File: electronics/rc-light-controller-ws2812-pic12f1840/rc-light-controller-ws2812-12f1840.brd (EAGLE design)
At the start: 33.7 x 10.2 mm, 13 parts, among them U1 12F1840

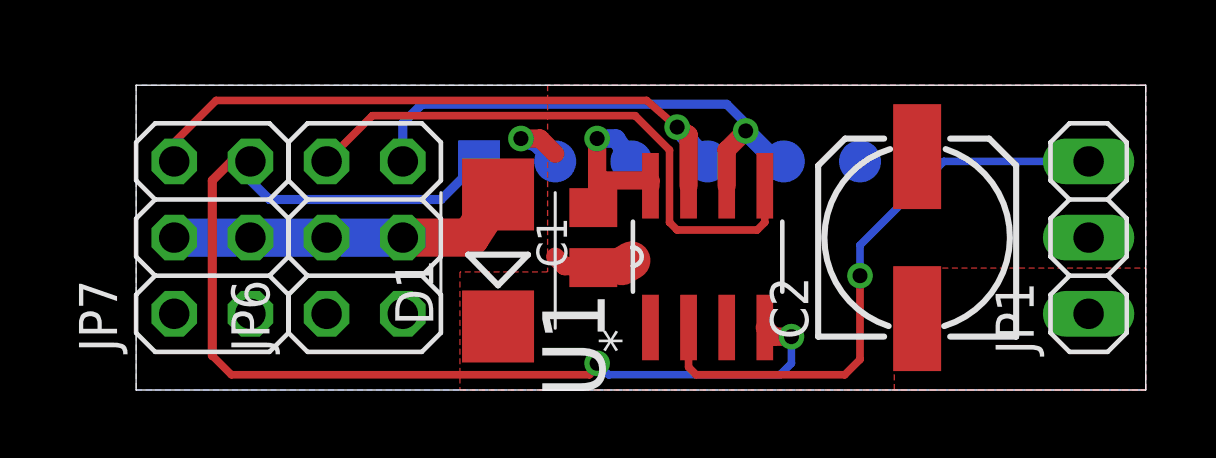
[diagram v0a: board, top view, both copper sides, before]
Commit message: Finish breakout board, tweak light controller board
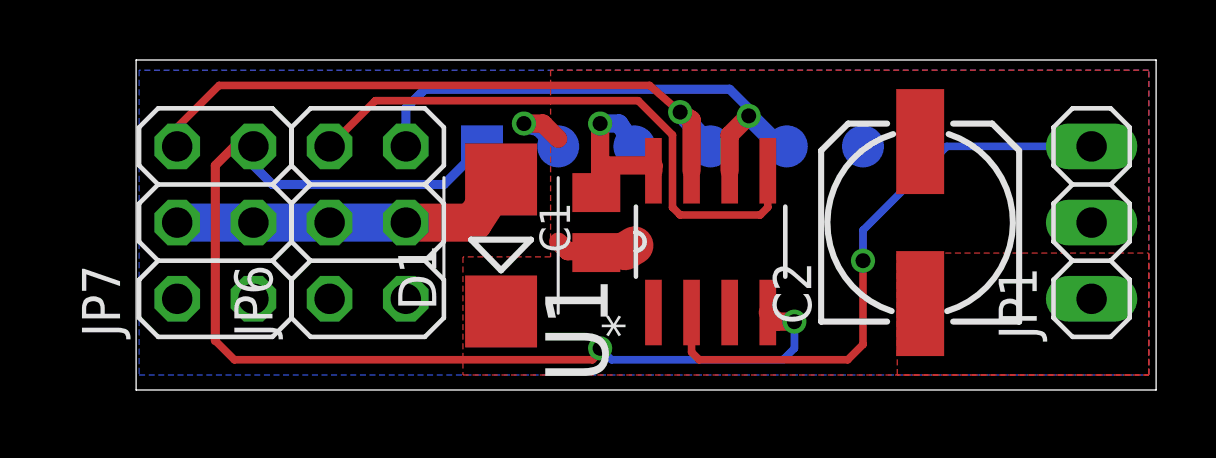
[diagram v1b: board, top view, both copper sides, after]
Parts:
- moved C2 0.51 mm to (26.1, 5.58)
- moved JP1 0.51 mm to (31.9, 5.58)
- moved JP7 0.51 mm to (2.64, 5.58)
- moved C1 0.51 mm to (15.3, 5.58)
- moved D1 0.51 mm to (12.2, 4.82)
- moved JP6 0.51 mm to (7.72, 5.58)
- moved U1 0.51 mm to (19.1, 4.95)
- moved CLK 0.51 mm to (21.7, 8.12)
- moved NC 0.51 mm to (24.2, 8.12)
- moved VDD 0.51 mm to (14.1, 8.12)
- moved VPP 0.51 mm to (11.5, 8.12)
- moved DAT 0.51 mm to (19.1, 8.12)
- moved GND 0.51 mm to (16.6, 8.12)
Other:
- board size 33.7 x 10.2 mm -> 34 x 11 mm
- board text added: "*"
- board text added: "-"
